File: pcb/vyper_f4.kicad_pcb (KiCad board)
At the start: 2 copper layers, 36 x 36 mm, 31 parts, among them J1 J1_usbc, J2 J2_esc_SH8, M1 PAD_M1, M2 PAD_M2, M3 PAD_M3, M4 PAD_M4, T2 PAD_T2, T4 PAD_T4, T6 PAD_T6, U1 U1_mcu_STM32F405RGT6, U2 U2_gyro_ICM42688P, U3 U3_buck_TPS54331, U4 U4_ldo_3v3, U5 U5_osd_AT7456E, U6 U6_flash_W25Q128, U7 U7_baro_BMP280, Y1 Y1_xtal_8MHz

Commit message: Build VYPER 200 kmh screening prototype
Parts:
- U3: value U3_buck_TPS54331 -> U3_buck_TPS54360; footprint VYPER:U3_buck_TPS54331 -> VYPER:U3_buck_TPS54360
- U5: value U5_osd_AT7456E -> U5_gyro_ldo_AP2112K; footprint VYPER:U5_osd_AT7456E -> VYPER:U5_gyro_ldo_AP2112K
- moved U5 7.38 mm to (7.00, -6.00)
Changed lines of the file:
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@@
 		(pad "1" smd roundrect (at 0.000 0.000) (size 2.0 2.0) (layers "F.Cu" "F.Paste" "F.Mask") (roundrect_rratio 0.25))
 	)
-	(gr_rect (start 7.300 -9.250) (end 15.300 9.250) (stroke (width 0.05) (type solid)) (fill no) (layer "F.CrtYd"))
-	(gr_rect (start 7.300 -9.250) (end 15.300 9.250) (stroke (width 0.12) (type solid)) (fill no) (layer "F.SilkS"))
-	(footprint "VYPER:U5_osd_AT7456E" (layer "F.Cu")
-		(at 11.300 -0.000)
+	(gr_rect (start 5.300 -7.600) (end 8.700 -4.400) (stroke (width 0.05) (type solid)) (fill no) (layer "F.CrtYd"))
+	(gr_rect (start 5.300 -7.600) (end 8.700 -4.400) (stroke (width 0.12) (type solid)) (fill no) (layer "F.SilkS"))
+	(footprint "VYPER:U5_gyro_ldo_AP2112K" (layer "F.Cu")
+		(at 7.000 -6.000)
 		(attr exclude_from_pos_files)
 		(property "Reference" "U5" (at 0 -2.4 0) (layer "F.SilkS")
 			(effects (font (size 0.8 0.8) (thickness 0.12)))
 		)
-		(property "Value" "U5_osd_AT7456E" (at 0 2.4 0) (layer "F.SilkS")
+		(property "Value" "U5_gyro_ldo_AP2112K" (at 0 2.4 0) (layer "F.SilkS")
 			(effects (font (size 0.5 0.5) (thickness 0.08)) (hide yes))
 		)
@@
 	(gr_rect (start 4.100 -15.800) (end 10.300 -10.600) (stroke (width 0.05) (type solid)) (fill no) (layer "F.CrtYd"))
 	(gr_rect (start 4.100 -15.800) (end 10.300 -10.600) (stroke (width 0.12) (type solid)) (fill no) (layer "F.SilkS"))
-	(footprint "VYPER:U3_buck_TPS54331" (layer "F.Cu")
+	(footprint "VYPER:U3_buck_TPS54360" (layer "F.Cu")
 		(at 7.200 -13.200)
 		(attr exclude_from_pos_files)
@@
 			(effects (font (size 0.8 0.8) (thickness 0.12)))
 		)
-		(property "Value" "U3_buck_TPS54331" (at 0 2.4 0) (layer "F.SilkS")
+		(property "Value" "U3_buck_TPS54360" (at 0 2.4 0) (layer "F.SilkS")
 			(effects (font (size 0.5 0.5) (thickness 0.08)) (hide yes))
 		)

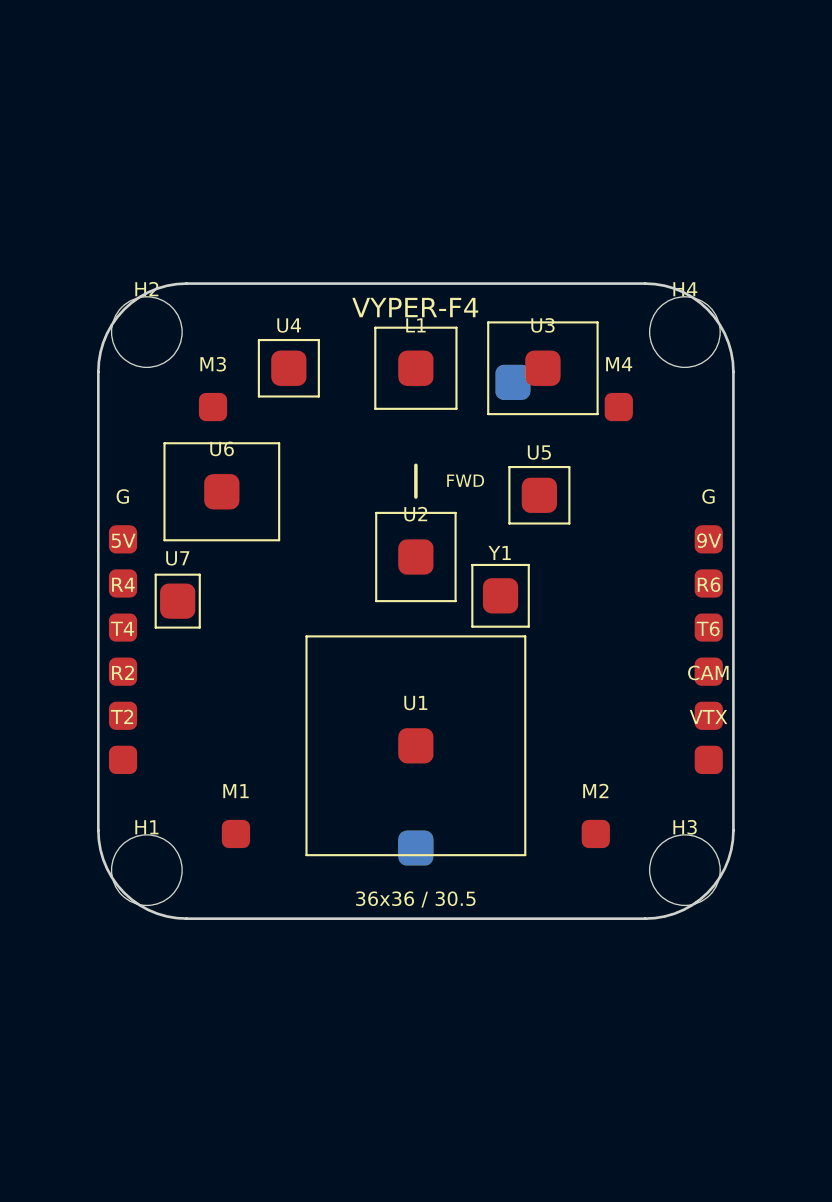
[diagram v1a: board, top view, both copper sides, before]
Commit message: Build true-footprint VYPER flight controller review board
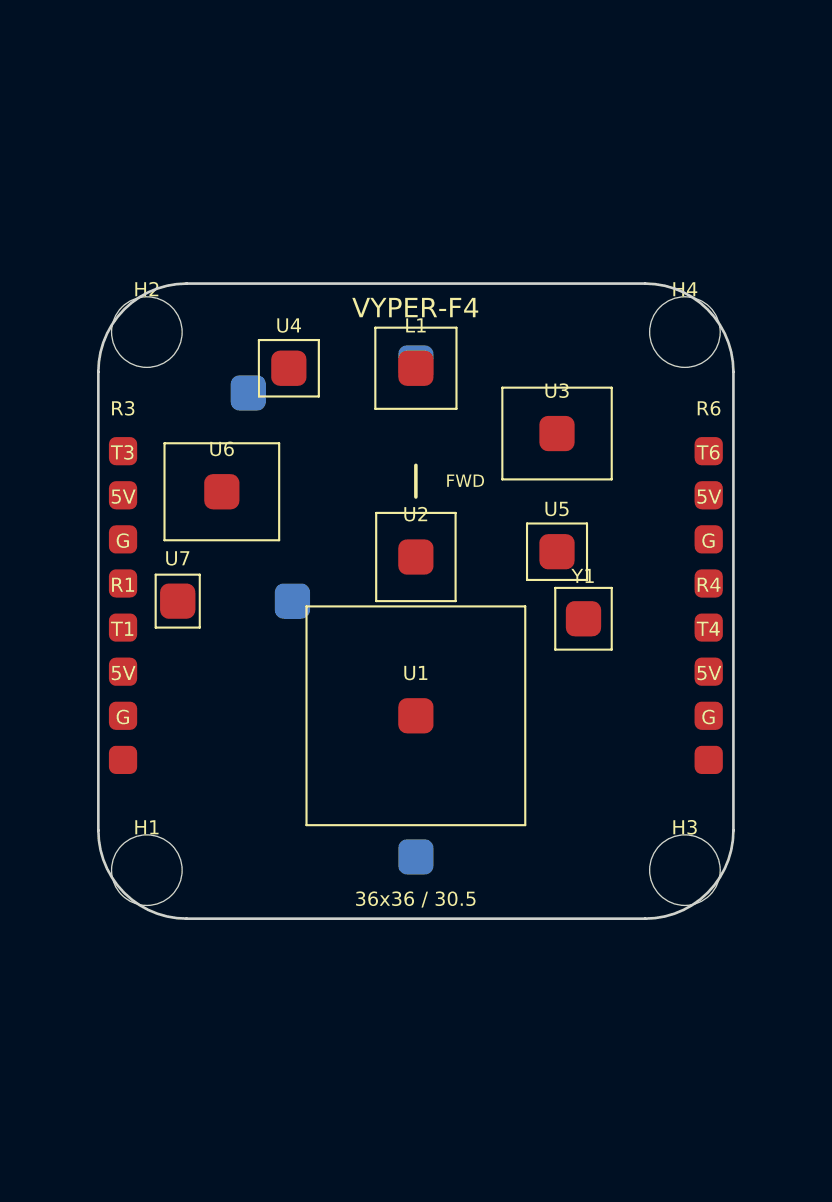
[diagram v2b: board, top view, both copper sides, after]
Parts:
- removed the 5V at (-16.6, -1.00)
- removed 9V: PAD_9V, VYPER:PAD_9V
- removed CAM: PAD_CAM, VYPER:PAD_CAM
- removed the G at (-16.6, -3.50)
- removed the G at (16.6, -3.50)
- removed M1: PAD_M1, VYPER:PAD_M1
- removed M2: PAD_M2, VYPER:PAD_M2
- removed M3: PAD_M3, VYPER:PAD_M3
- removed M4: PAD_M4, VYPER:PAD_M4
- removed R2: PAD_R2, VYPER:PAD_R2
- removed T2: PAD_T2, VYPER:PAD_T2
- removed VTX: PAD_VTX, VYPER:PAD_VTX
- added 5V: PAD_5V, VYPER:PAD_5V, F.Cu at (-16.6, 6.50)
- added 5V: PAD_5V, VYPER:PAD_5V, F.Cu at (-16.6, -3.50)
- added 5V: PAD_5V, VYPER:PAD_5V, F.Cu at (16.6, 6.50)
- added 5V: PAD_5V, VYPER:PAD_5V, F.Cu at (16.6, -3.50)
- added G: PAD_G, VYPER:PAD_G, F.Cu at (-16.6, 9.00)
- added G: PAD_G, VYPER:PAD_G, F.Cu at (-16.6, -1.00)
- added G: PAD_G, VYPER:PAD_G, F.Cu at (16.6, 9.00)
- added G: PAD_G, VYPER:PAD_G, F.Cu at (16.6, -1.00)
- added J7: J7_swd_testpads, VYPER:J7_swd_testpads, B.Cu at (-7.00, -0.00)
- added J8: J8_beeper_pads, VYPER:J8_beeper_pads, B.Cu at (-9.50, -11.8)
- added R1: PAD_R1, VYPER:PAD_R1, F.Cu at (-16.6, 1.50)
- added R3: PAD_R3, VYPER:PAD_R3, F.Cu at (-16.6, -8.50)
- added T1: PAD_T1, VYPER:PAD_T1, F.Cu at (-16.6, 4.00)
- added T3: PAD_T3, VYPER:PAD_T3, F.Cu at (-16.6, -6.00)
- J1: value J1_usbc -> J1_usb_service_SH4; footprint VYPER:J1_usbc -> VYPER:J1_usb_service_SH4
- moved R4 33.2 mm to (16.6, 1.50)
- moved T4 33.2 mm to (16.6, 4.00)
- moved R6 10.0 mm to (16.6, -8.50)
- moved T6 10.0 mm to (16.6, -6.00)
- moved J2 5.61 mm to (0.00, -13.5)
- moved Y1 4.88 mm to (9.50, 1.00)
- moved U3 3.79 mm to (8.00, -9.50)
- moved U5 3.35 mm to (8.00, -2.80)
- moved U1 1.70 mm to (0.00, 6.50)
- moved J1 0.50 mm to (0.00, 14.5)

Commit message: Place all VYPER FC passives in verified 43 mm layout
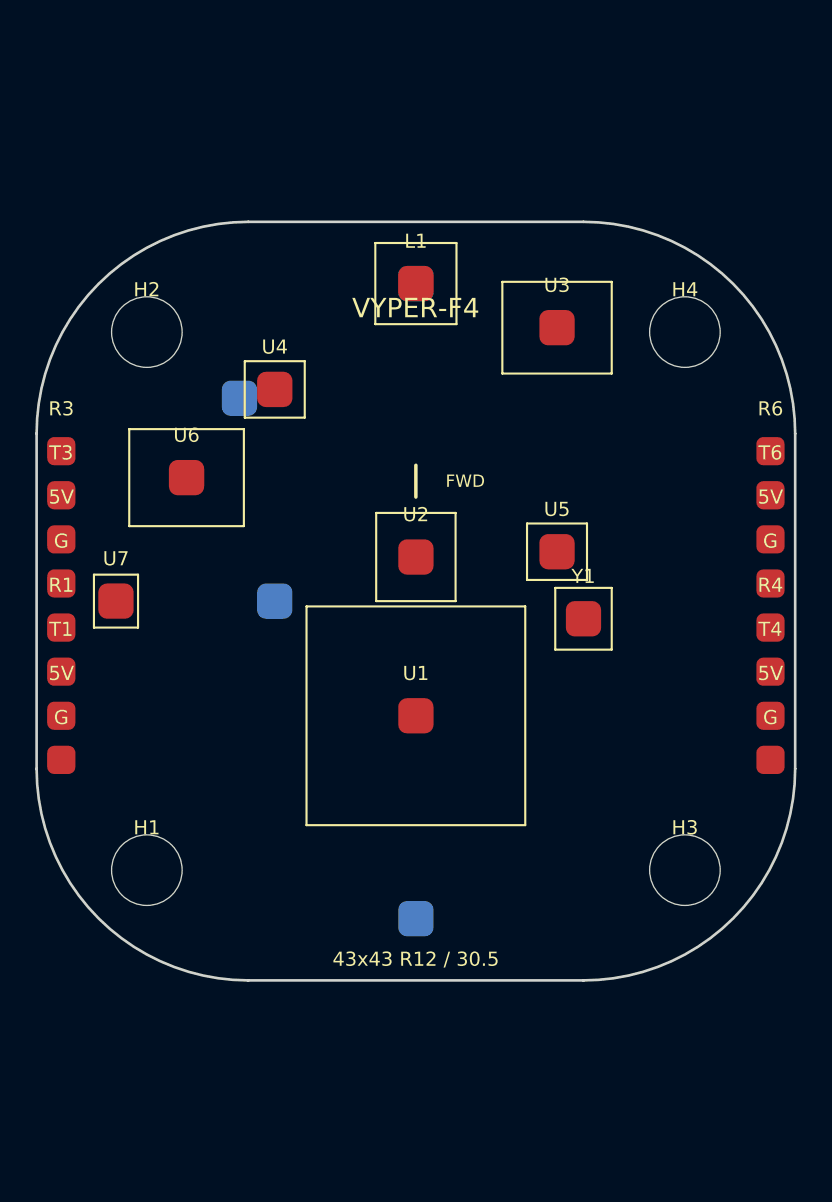
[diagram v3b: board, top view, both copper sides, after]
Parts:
- removed the 5V at (-16.6, 6.50)
- removed the 5V at (-16.6, -3.50)
- removed the 5V at (16.6, 6.50)
- removed the 5V at (16.6, -3.50)
- removed the G at (-16.6, 9.00)
- removed the G at (-16.6, -1.00)
- removed the G at (16.6, 9.00)
- removed the G at (16.6, -1.00)
- added 5V: PAD_5V, VYPER:PAD_5V, F.Cu at (-20.1, 6.50)
- added 5V: PAD_5V, VYPER:PAD_5V, F.Cu at (-20.1, -3.50)
- added 5V: PAD_5V, VYPER:PAD_5V, F.Cu at (20.1, 6.50)
- added 5V: PAD_5V, VYPER:PAD_5V, F.Cu at (20.1, -3.50)
- added G: PAD_G, VYPER:PAD_G, F.Cu at (-20.1, 9.00)
- added G: PAD_G, VYPER:PAD_G, F.Cu at (-20.1, -1.00)
- added G: PAD_G, VYPER:PAD_G, F.Cu at (20.1, 9.00)
- added G: PAD_G, VYPER:PAD_G, F.Cu at (20.1, -1.00)
- moved U3 6.00 mm to (8.00, -15.5)
- moved L1 4.80 mm to (0.00, -18.0)
- moved J2 4.50 mm to (0.00, -18.0)
- moved J1 3.50 mm to (0.00, 18.0)
- moved R1 3.50 mm to (-20.1, 1.50)
- moved R3 3.50 mm to (-20.1, -8.50)
- moved R4 3.50 mm to (20.1, 1.50)
- moved R6 3.50 mm to (20.1, -8.50)
- moved T1 3.50 mm to (-20.1, 4.00)
- moved T3 3.50 mm to (-20.1, -6.00)
- moved T4 3.50 mm to (20.1, 4.00)
- moved T6 3.50 mm to (20.1, -6.00)
- moved U7 3.50 mm to (-17.0, -0.00)
- moved U6 2.15 mm to (-13.0, -7.00)
- moved U4 1.44 mm to (-8.00, -12.0)
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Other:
- board size 36 x 36 mm -> 43 x 43 mm
- board text added: "43x43 R12 / 30.5"
- board text removed: "36x36 / 30.5"

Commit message: Redesign VYPER around vertical dense electronics
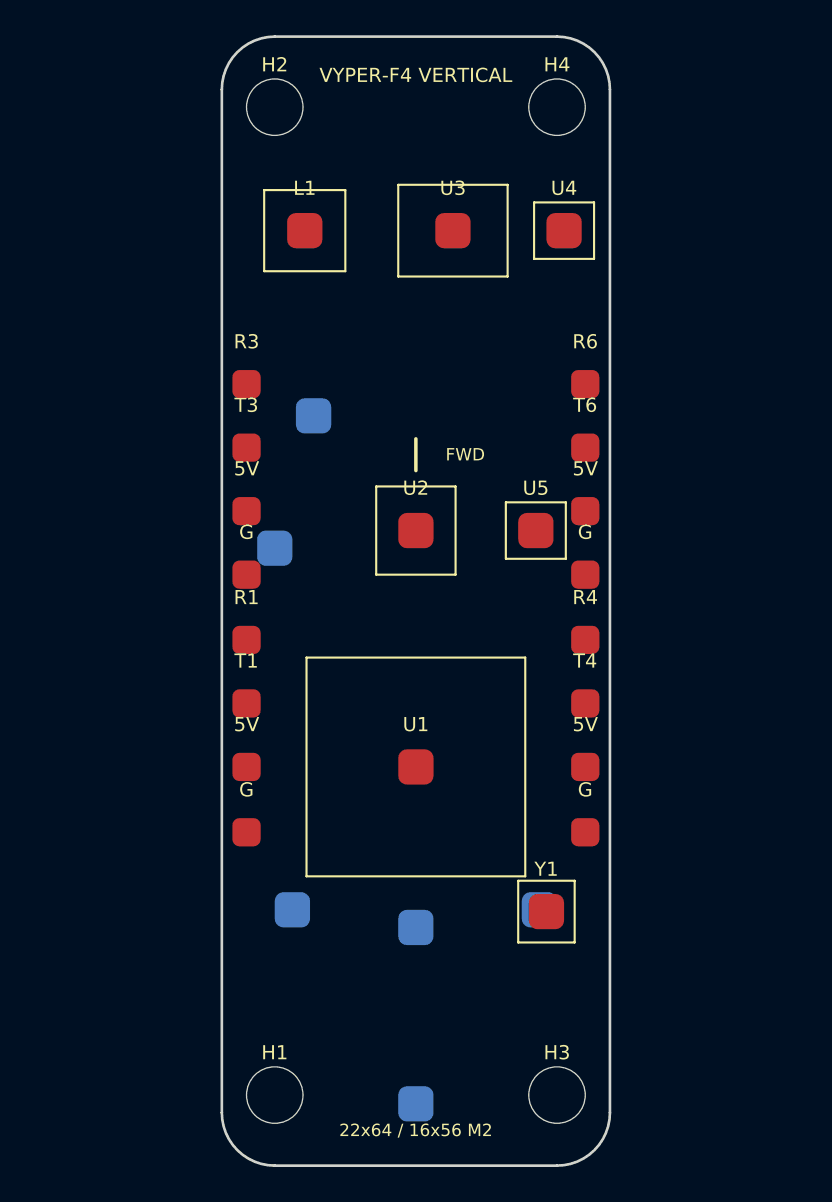
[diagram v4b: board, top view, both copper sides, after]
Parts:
- removed the 5V at (-20.1, 6.50)
- removed the 5V at (-20.1, -3.50)
- removed the 5V at (20.1, 6.50)
- removed the 5V at (20.1, -3.50)
- removed the G at (-20.1, 9.00)
- removed the G at (-20.1, -1.00)
- removed the G at (20.1, 9.00)
- removed the G at (20.1, -1.00)
- added 5V: PAD_5V, VYPER:PAD_5V, F.Cu at (-9.60, 9.40)
- added 5V: PAD_5V, VYPER:PAD_5V, F.Cu at (-9.60, -5.10)
- added 5V: PAD_5V, VYPER:PAD_5V, F.Cu at (9.60, 9.40)
- added 5V: PAD_5V, VYPER:PAD_5V, F.Cu at (9.60, -5.10)
- added G: PAD_G, VYPER:PAD_G, F.Cu at (-9.60, 13.1)
- added G: PAD_G, VYPER:PAD_G, F.Cu at (-9.60, -1.50)
- added G: PAD_G, VYPER:PAD_G, F.Cu at (9.60, 13.1)
- added G: PAD_G, VYPER:PAD_G, F.Cu at (9.60, -1.50)
- U6, U7: moved to B.Cu
- moved J2 36.5 mm to (0.00, 18.5)
- moved J8 33.6 mm to (7.00, 17.5)
- moved U4 18.7 mm to (8.40, -21.0)
- moved J7 17.5 mm to (-7.00, 17.5)
- moved Y1 16.7 mm to (7.40, 17.6)
- moved H1 14.7 mm to (-8.00, 28.0)
- moved H2 14.7 mm to (-8.00, -28.0)
- moved H3 14.7 mm to (8.00, 28.0)
- moved H4 14.7 mm to (8.00, -28.0)
- moved R3 11.2 mm to (-9.60, -12.3)
- moved R6 11.2 mm to (9.60, -12.3)
- moved T3 10.8 mm to (-9.60, -8.70)
- moved T6 10.8 mm to (9.60, -8.70)
- moved T1 10.7 mm to (-9.60, 5.80)
- moved T4 10.7 mm to (9.60, 5.80)
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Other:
- board size 43 x 43 mm -> 22 x 64 mm
- board text added: "22x64 / 16x56 M2"
- board text added: "VYPER-F4 VERTICAL"
- board text removed: "43x43 R12 / 30.5"
- board text removed: "VYPER-F4"

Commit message: Add production-size wire pads and reproducible PETG slicing
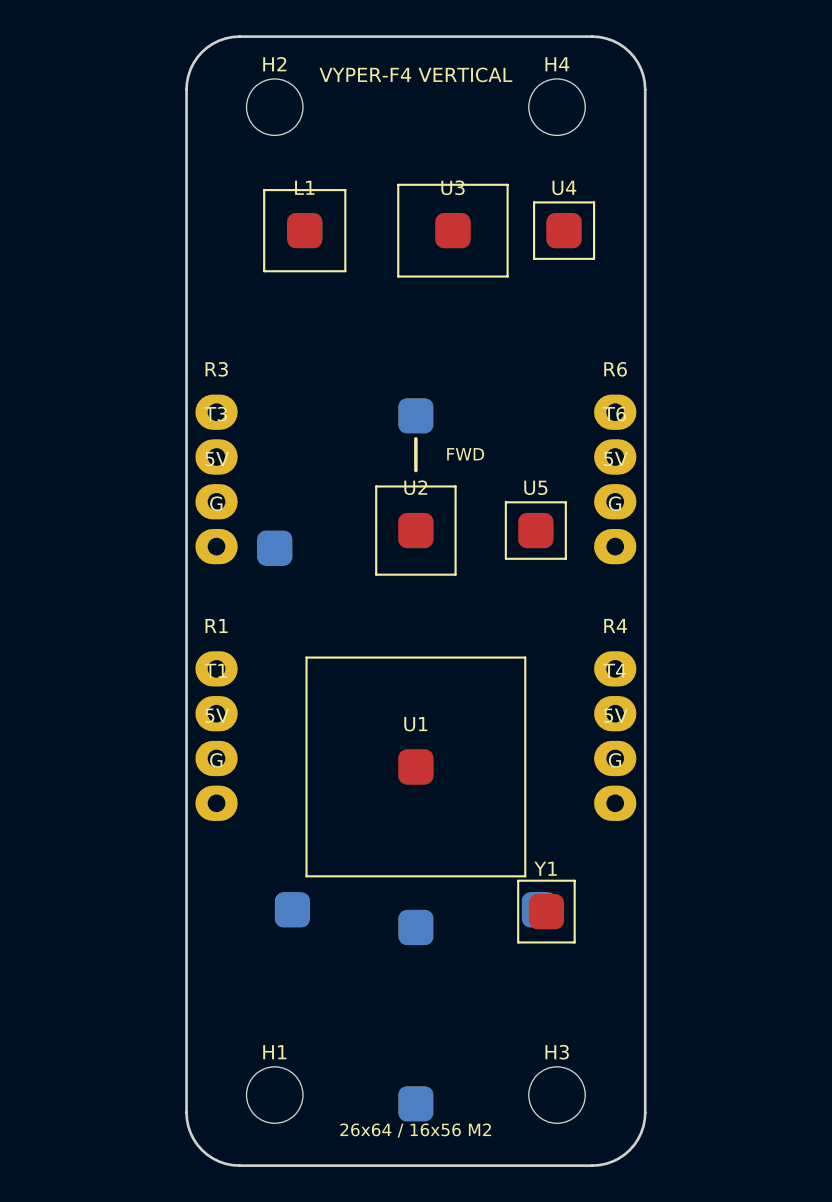
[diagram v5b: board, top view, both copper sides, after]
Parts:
- removed the 5V at (-9.60, 9.40)
- removed the 5V at (-9.60, -5.10)
- removed the 5V at (9.60, 9.40)
- removed the 5V at (9.60, -5.10)
- removed the G at (-9.60, 13.1)
- removed the G at (-9.60, -1.50)
- removed the G at (9.60, 13.1)
- removed the G at (9.60, -1.50)
- added 5V: PAD_5V, VYPER:PAD_5V, F.Cu at (-11.3, 8.92)
- added 5V: PAD_5V, VYPER:PAD_5V, F.Cu at (-11.3, -5.63)
- added 5V: PAD_5V, VYPER:PAD_5V, F.Cu at (11.3, 8.92)
- added 5V: PAD_5V, VYPER:PAD_5V, F.Cu at (11.3, -5.63)
- added G: PAD_G, VYPER:PAD_G, F.Cu at (-11.3, 11.5)
- added G: PAD_G, VYPER:PAD_G, F.Cu at (-11.3, -3.09)
- added G: PAD_G, VYPER:PAD_G, F.Cu at (11.3, 11.5)
- added G: PAD_G, VYPER:PAD_G, F.Cu at (11.3, -3.09)
- moved U6 5.80 mm to (0.00, -10.5)
- moved R1 2.36 mm to (-11.3, 3.84)
- moved R4 2.36 mm to (11.3, 3.84)
- moved R3 2.33 mm to (-11.3, -10.7)
- moved R6 2.33 mm to (11.3, -10.7)
- moved T1 1.80 mm to (-11.3, 6.38)
- moved T4 1.80 mm to (11.3, 6.38)
- moved T3 1.78 mm to (-11.3, -8.17)
- moved T6 1.78 mm to (11.3, -8.17)
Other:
- board size 22 x 64 mm -> 26 x 64 mm
- board text added: "26x64 / 16x56 M2"
- board text removed: "22x64 / 16x56 M2"

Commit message: Redesign Vyper FC with sensors and RGB
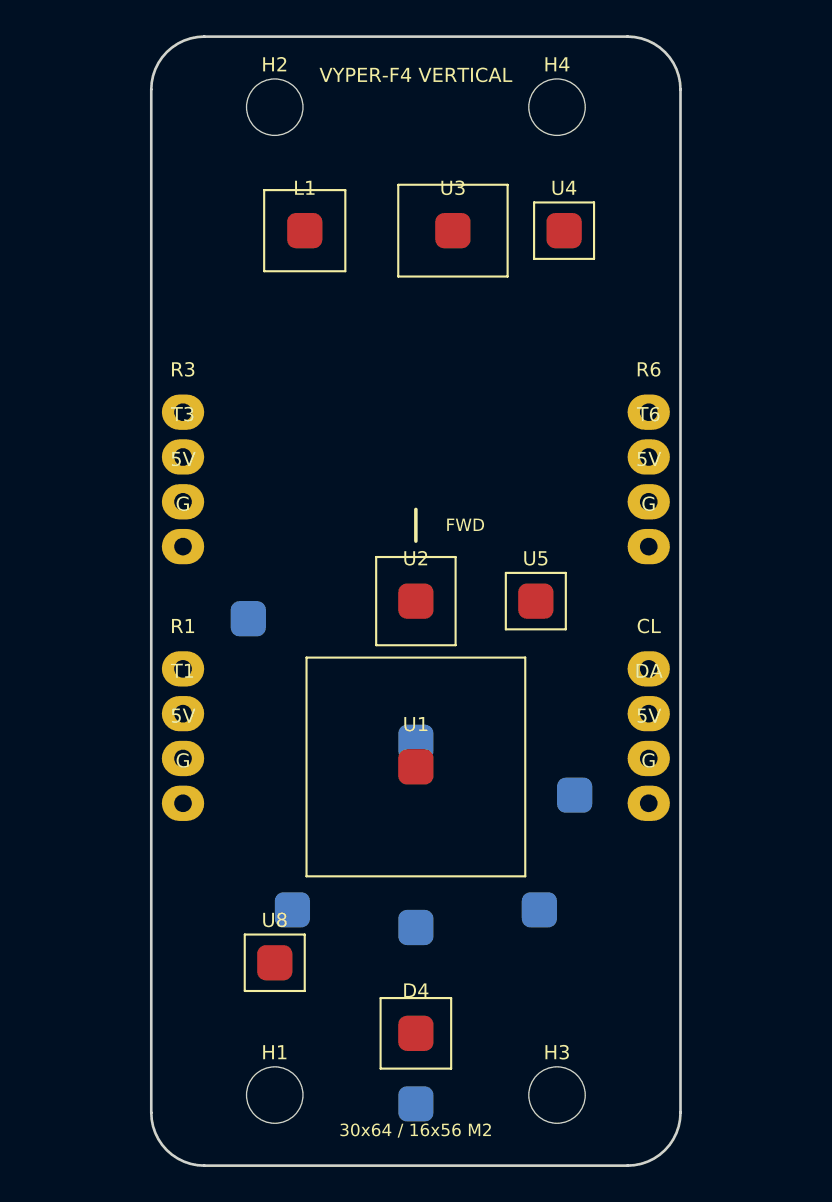
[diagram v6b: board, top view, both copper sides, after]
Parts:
- removed the 5V at (-11.3, 8.92)
- removed the 5V at (-11.3, -5.63)
- removed the 5V at (11.3, 8.92)
- removed the 5V at (11.3, -5.63)
- removed the G at (-11.3, 11.5)
- removed the G at (-11.3, -3.09)
- removed the G at (11.3, 11.5)
- removed the G at (11.3, -3.09)
- removed R4: PAD_R4, VYPER:PAD_R4
- removed T4: PAD_T4, VYPER:PAD_T4
- added 5V: PAD_5V, VYPER:PAD_5V, F.Cu at (-13.2, 8.92)
- added 5V: PAD_5V, VYPER:PAD_5V, F.Cu at (-13.2, -5.63)
- added 5V: PAD_5V, VYPER:PAD_5V, F.Cu at (13.2, 8.92)
- added 5V: PAD_5V, VYPER:PAD_5V, F.Cu at (13.2, -5.63)
- added CL: PAD_CL, VYPER:PAD_CL, F.Cu at (13.2, 3.84)
- added D4: D4_rgb_status, VYPER:D4_rgb_status, F.Cu at (0.00, 24.5)
- added DA: PAD_DA, VYPER:PAD_DA, F.Cu at (13.2, 6.38)
- added G: PAD_G, VYPER:PAD_G, F.Cu at (-13.2, 11.5)
- added G: PAD_G, VYPER:PAD_G, F.Cu at (-13.2, -3.09)
- added G: PAD_G, VYPER:PAD_G, F.Cu at (13.2, 11.5)
- added G: PAD_G, VYPER:PAD_G, F.Cu at (13.2, -3.09)
- added U8: U8_rgb_level_shifter, VYPER:U8_rgb_level_shifter, F.Cu at (-8.00, 20.5)
- Y1: moved to B.Cu
- moved U6 18.5 mm to (0.00, 8.00)
- moved Y1 6.79 mm to (9.00, 11.0)
- moved U7 4.27 mm to (-9.50, 1.00)
- moved U2 4.00 mm to (0.00, -0.00)
- moved U5 4.00 mm to (6.80, -0.00)
- moved R1 1.90 mm to (-13.2, 3.84)
- moved R3 1.90 mm to (-13.2, -10.7)
- moved R6 1.90 mm to (13.2, -10.7)
- moved T1 1.90 mm to (-13.2, 6.38)
- moved T3 1.90 mm to (-13.2, -8.17)
- moved T6 1.90 mm to (13.2, -8.17)
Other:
- board size 26 x 64 mm -> 30 x 64 mm
- board text added: "30x64 / 16x56 M2"
- board text removed: "26x64 / 16x56 M2"
